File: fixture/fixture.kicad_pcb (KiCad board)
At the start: 2 copper layers, 100 x 100 mm, 40 parts, among them J1 Conn_Coaxial, J10 Conn_Coaxial, J11 Conn_Coaxial, J12 Conn_Coaxial, J13 Conn_Coaxial, J14 Conn_Coaxial, J15 Conn_Coaxial, J16 Conn_Coaxial, J17 Conn_Coaxial, J18 Conn_01x01, J19 Conn_01x01, J2 Conn_Coaxial, J20 Conn_01x01, J21 Conn_01x01, J22 Conn_Coaxial, J23 Conn_Coaxial, J24 Conn_Coaxial, J25 Conn_Coaxial, J26 Conn_01x02, J27 Conn_Coaxial, J28 Conn_01x02, J29 Conn_Coaxial, J3 Conn_Coaxial, J30 Conn_01x01, J31 Conn_01x01, J32 Conn_Coaxial, J4 Conn_02x08_Counter_Clockwise, J5 Conn_02x08_Counter_Clockwise, J6 Conn_Coaxial, J7 Conn_Coaxial, J8 Conn_Coaxial, J9 Conn_Coaxial

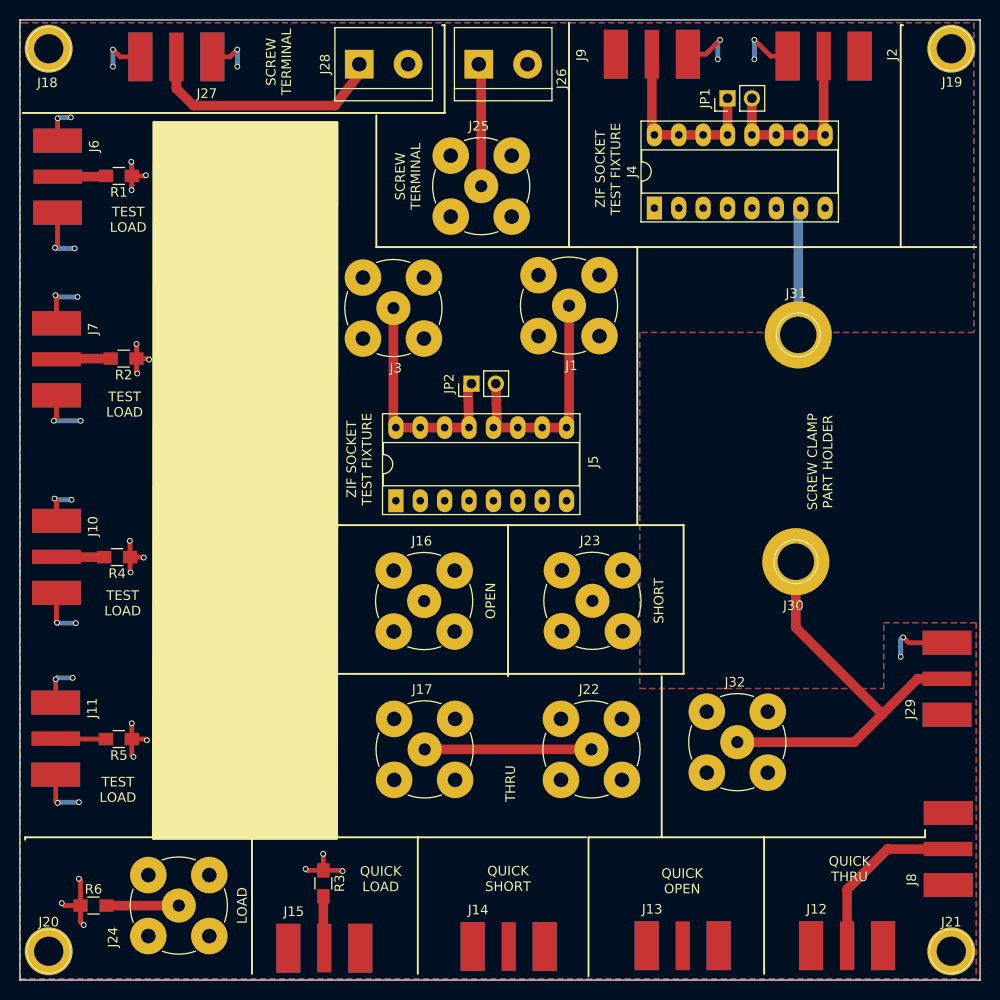
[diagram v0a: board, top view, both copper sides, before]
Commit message: Added area around open circuit without copper fill
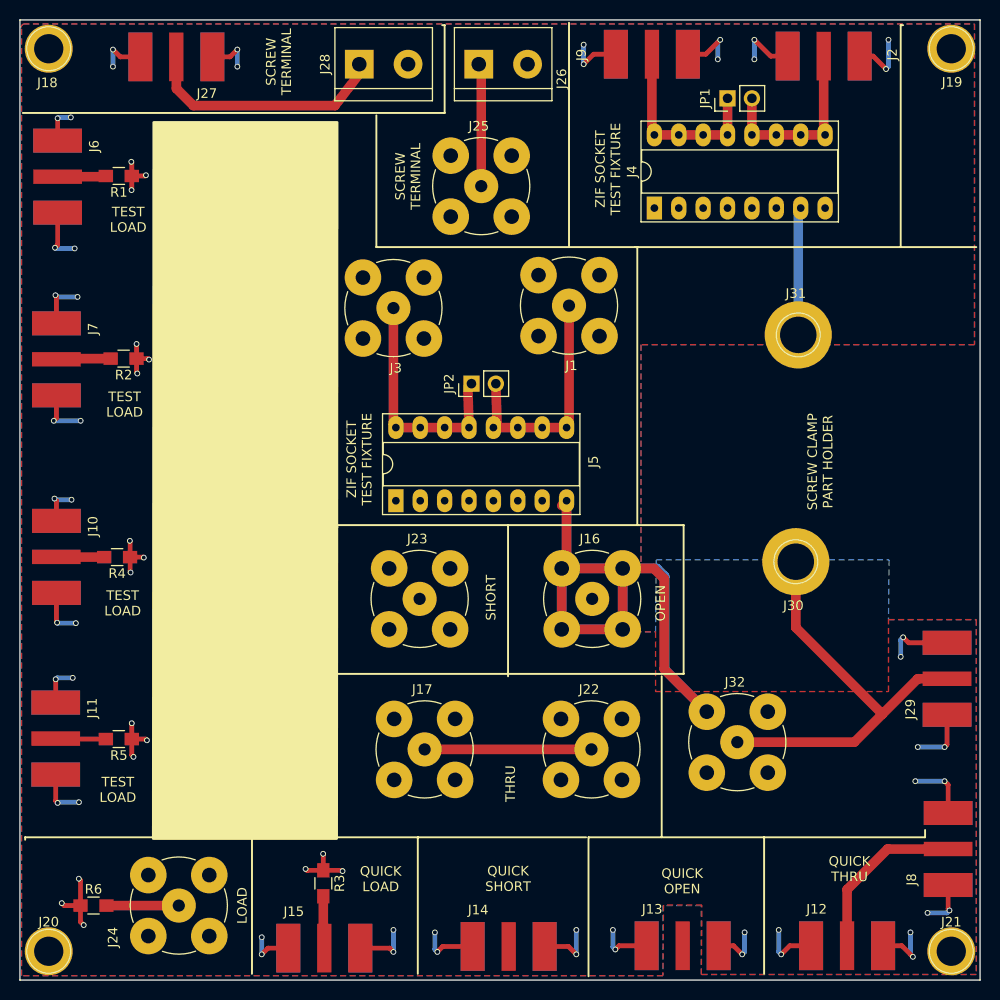
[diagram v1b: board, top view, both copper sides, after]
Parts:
- moved J23 18.0 mm to (91.6, 110.3)
- moved J16 17.5 mm to (109.6, 110.3)
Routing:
- net GND: track 114.0 -> 297.3 mm, vias 44 -> 70
